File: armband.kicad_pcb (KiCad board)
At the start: 6 copper layers, 151.9 x 110.6 mm, 86 parts, among them IC1 QSMP-1570, IC10 TLE493DW2B6A0HTSA1, IC2 BMI323, IC3 TPS259571DSGR, IC4 TPD6E001RSERG4, IC5 MP2722GRH-0000-Z, IC6 TPS62291DRVR, IC7 TPS62293DRVR, IC8 BQ27427YZFR, IC9 nRF52832-CIAA-G-R7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

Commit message: progressed layout
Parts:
- moved L4 21.9 mm to (149.3, 81.0), turned to 90 degrees
- moved L5 16.3 mm to (149.3, 82.9), turned to 180 degrees
- moved Y2 15.5 mm to (152.8, 83.4)
- moved L6 14.9 mm to (155.4, 79.7), turned to 180 degrees
- moved C33 14.8 mm to (148.1, 82.3), turned to -90 degrees
- moved C32 14.7 mm to (150.4, 82.1), turned to -90 degrees
- moved IC9 14.6 mm to (151.8, 79.5), turned to 180 degrees
- moved C31 13.9 mm to (148.6, 78.6), turned to 90 degrees
- moved C38 13.9 mm to (151.3, 83.6), turned to 90 degrees
- moved C34 13.0 mm to (149.6, 78.6), turned to 90 degrees
- moved AE1 11.3 mm to (157.3, 81.8), turned to -90 degrees
- moved C39 11.1 mm to (154.0, 79.3), turned to 90 degrees
- moved C37 10.8 mm to (154.3, 83.2), turned to -90 degrees
- moved C35 10.8 mm to (151.7, 81.9), turned to 180 degrees
- moved C36 8.96 mm to (154.1, 81.4), turned to 90 degrees
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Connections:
- IC1 pad 19: MP2722_INT -> LCD_TE
- IC1 pad 20: BMI_INT1 -> LCD_RST
- IC1 pad 21: BMI_INT2 -> TP_INT
- IC1 pad 22: MAX_INT -> TP_RST
- IC1 pad 23: TP_INT -> QSMP_LCD_EN
- IC1 pad 24: TP_RST -> BMI_INT1
- IC1 pad 25: LCD_TE -> BMI_INT2
- IC1 pad 26: LCD_RST -> MAX_INT
- IC1 pad 27: QSMP_LCD_EN -> MP2722_INT
- IC9 pad E7: unconnected-(IC9-P0.05/_AIN3-PadE7) -> QSMP_SDA
- IC9 pad F4: QSMP_TXD_NRF -> unconnected-(IC9-P0.11-PadF4)
- IC9 pad F6: QSMP_SDA -> unconnected-(IC9-P0.07-PadF6)
- IC9 pad H3: unconnected-(IC9-P0.16_/TRACEDATA[1]-PadH3) -> QSMP_TXD_NRF
- IC9 pad H4: unconnected-(IC9-P0.15/TRACEDATA[2]-PadH4) -> QSMP_RXD_NRF
- IC9 pad H6: QSMP_RXD_NRF -> unconnected-(IC9-P0.12-PadH6)
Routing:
- net NFC_ANT1: track 0.00 -> 35.1 mm, vias 0 -> 2
- net NFC_ANT2: track 0.00 -> 34.7 mm, vias 0 -> 2
- net TP_INT: track 0.00 -> 33.4 mm, vias 0 -> 2
- net TP_RST: track 0.00 -> 33.4 mm, vias 0 -> 2
- net LCD_RST: track 0.00 -> 33.3 mm, vias 0 -> 2
- net LCD_TE: track 0.00 -> 33.3 mm, vias 0 -> 2
- net QSMP_LCD_EN: track 0.82 -> 32.2 mm, vias 1 -> 2
- net QSMP_RXD_NRF: track 0.00 -> 20.7 mm, vias 0 -> 1
- net QSMP_DCX: track 0.00 -> 19.9 mm, vias 0 -> 1
- net QSMP_TXD_NRF: track 0.00 -> 18.4 mm, vias 0 -> 1
- net QSMP_MISO: track 0.00 -> 14.8 mm, vias 0 -> 1
- net GND: track 4.24 -> 18.7 mm, vias 10 -> 26
- net QSMP_SCK: track 0.00 -> 13.2 mm, vias 0 -> 1
- net QSMP_MOSI: track 0.00 -> 11.9 mm, vias 0 -> 1
- net QSMP_SDA: track 42.3 -> 53.5 mm, vias 3 -> 5
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
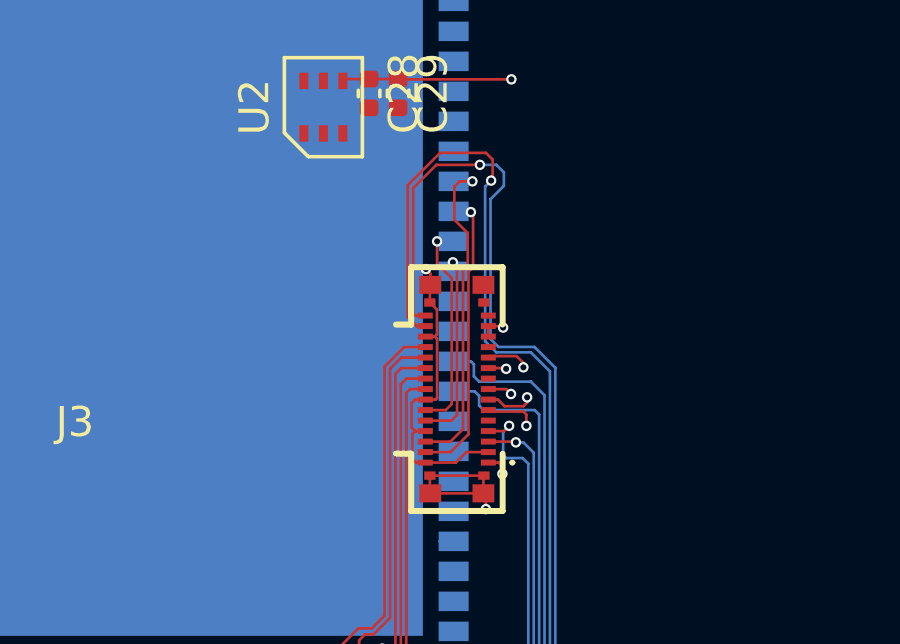
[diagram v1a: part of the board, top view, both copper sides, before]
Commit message: there was an attempt to length match DSI
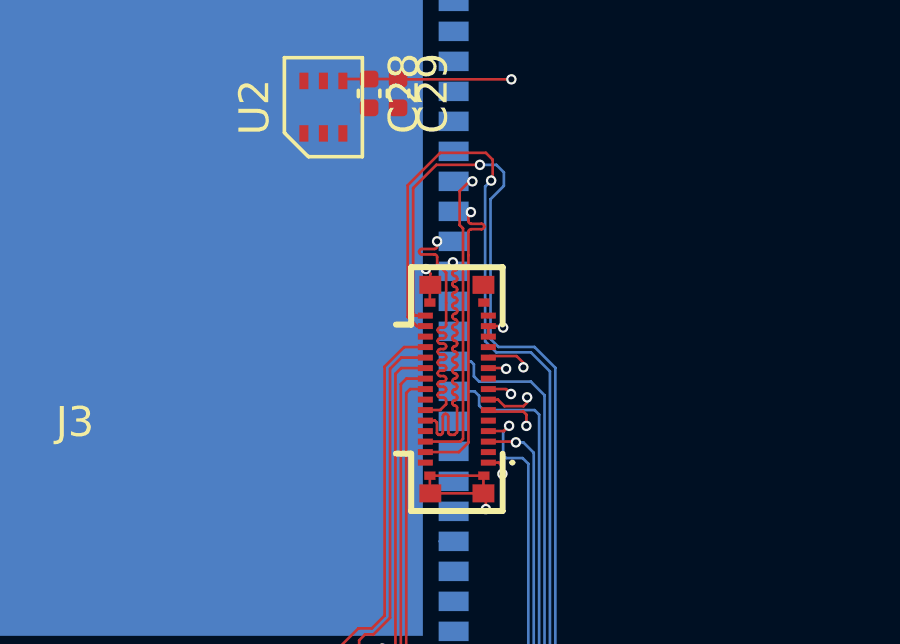
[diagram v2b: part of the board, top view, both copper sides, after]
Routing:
- net GND: track 18.7 -> 9.07 mm
- net QSMP_DSI_CLKN: track 6.59 -> 10.8 mm
- net QSMP_DSI_CLKP: track 7.14 -> 10.6 mm
- net QSMP_DSI_D0N: track 9.77 -> 10.8 mm

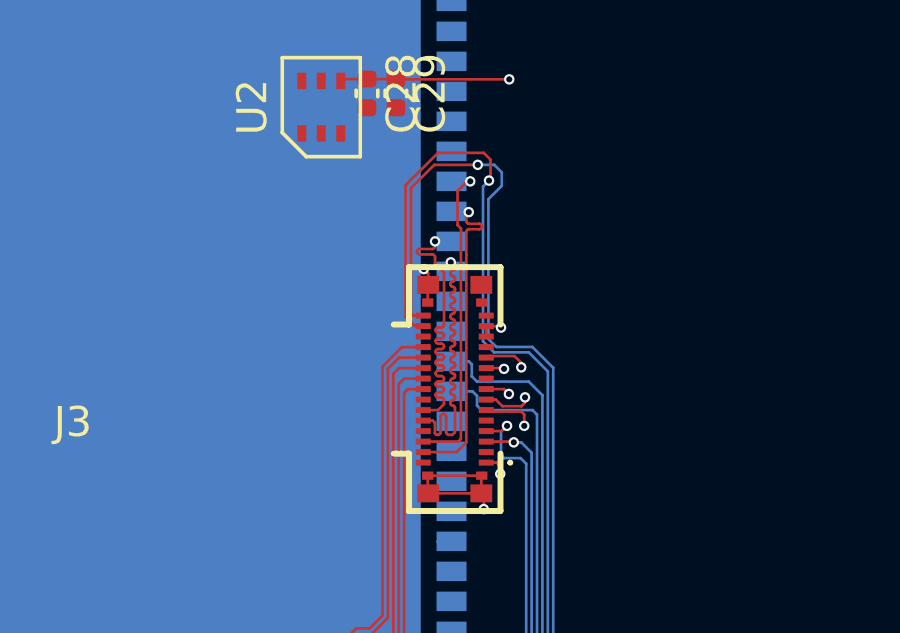
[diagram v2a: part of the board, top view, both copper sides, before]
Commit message: Update length matching
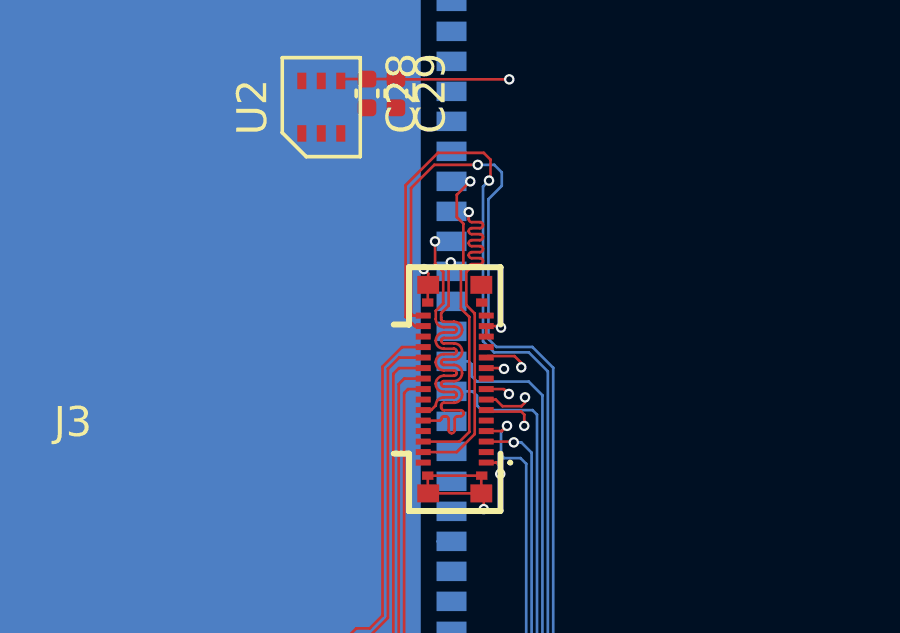
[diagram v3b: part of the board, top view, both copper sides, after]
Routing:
- net QSMP_DSI_D0N: track 10.8 -> 13.1 mm
- net QSMP_DSI_CLKN: track 10.8 -> 12.7 mm

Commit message: progressed layout
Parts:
- moved C10 0.90 mm to (138.8, 84.5)
- moved C11 0.90 mm to (131.8, 85.2)
- moved C12 0.90 mm to (131.8, 81.7)
- moved C13 0.90 mm to (133.5, 85.0)
- moved C14 0.90 mm to (133.5, 86.0)
- moved C15 0.90 mm to (142.8, 86.1)
- moved C16 0.90 mm to (144.7, 81.0)
- moved C17 0.90 mm to (131.8, 79.9)
- moved C21 0.90 mm to (131.8, 83.6)
- moved C22 0.90 mm to (127.6, 79.8)
- moved C23 0.90 mm to (129.0, 79.8)
- moved IC3 0.90 mm to (138.1, 82.7)
- moved IC4 0.90 mm to (141.8, 82.8)
- moved IC5 0.90 mm to (129.4, 82.7)
- moved IC6 0.90 mm to (144.7, 85.4)
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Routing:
- net VSYS: track 36.8 -> 37.7 mm
- net QSMP_SCL: track 52.6 -> 53.5 mm
- net NRF_NRST: track 0.33 -> 0.65 mm, vias 0 -> 1

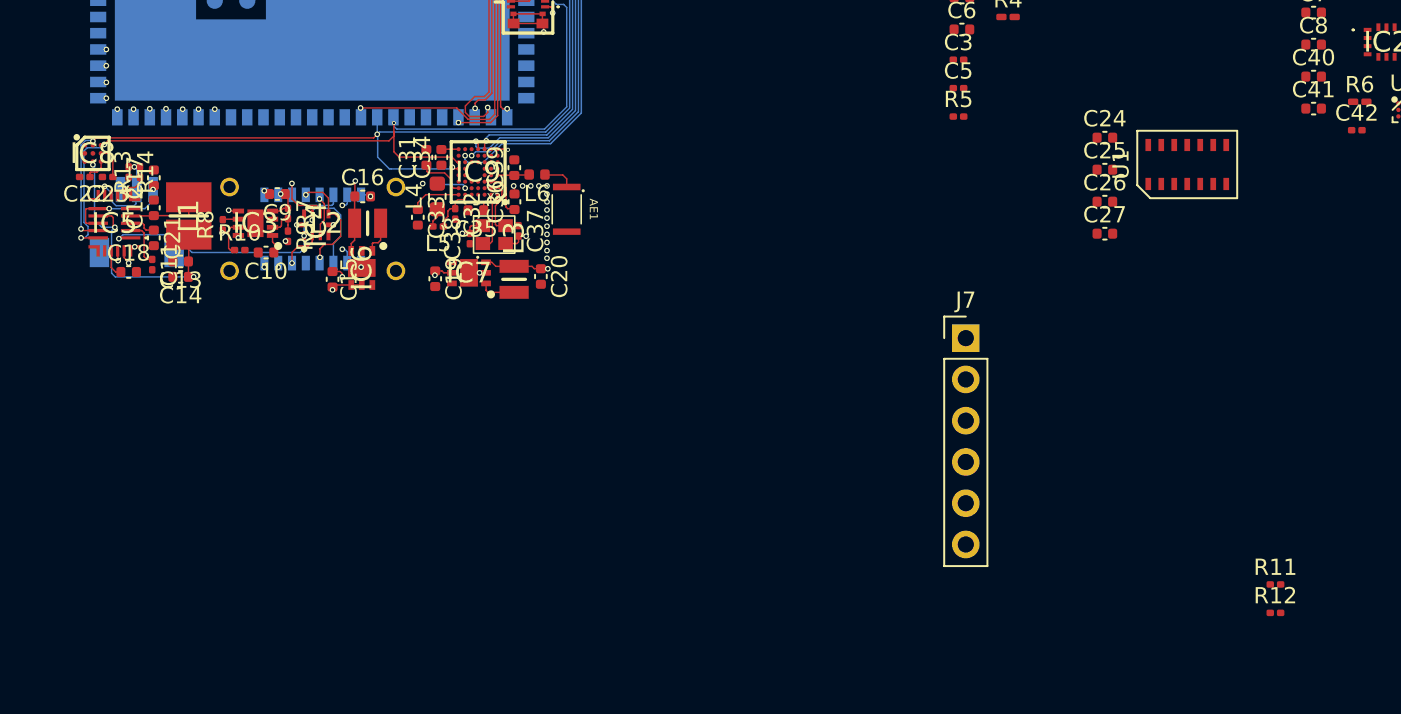
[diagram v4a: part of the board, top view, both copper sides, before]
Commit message: Add Heartbeat sensor to PCB
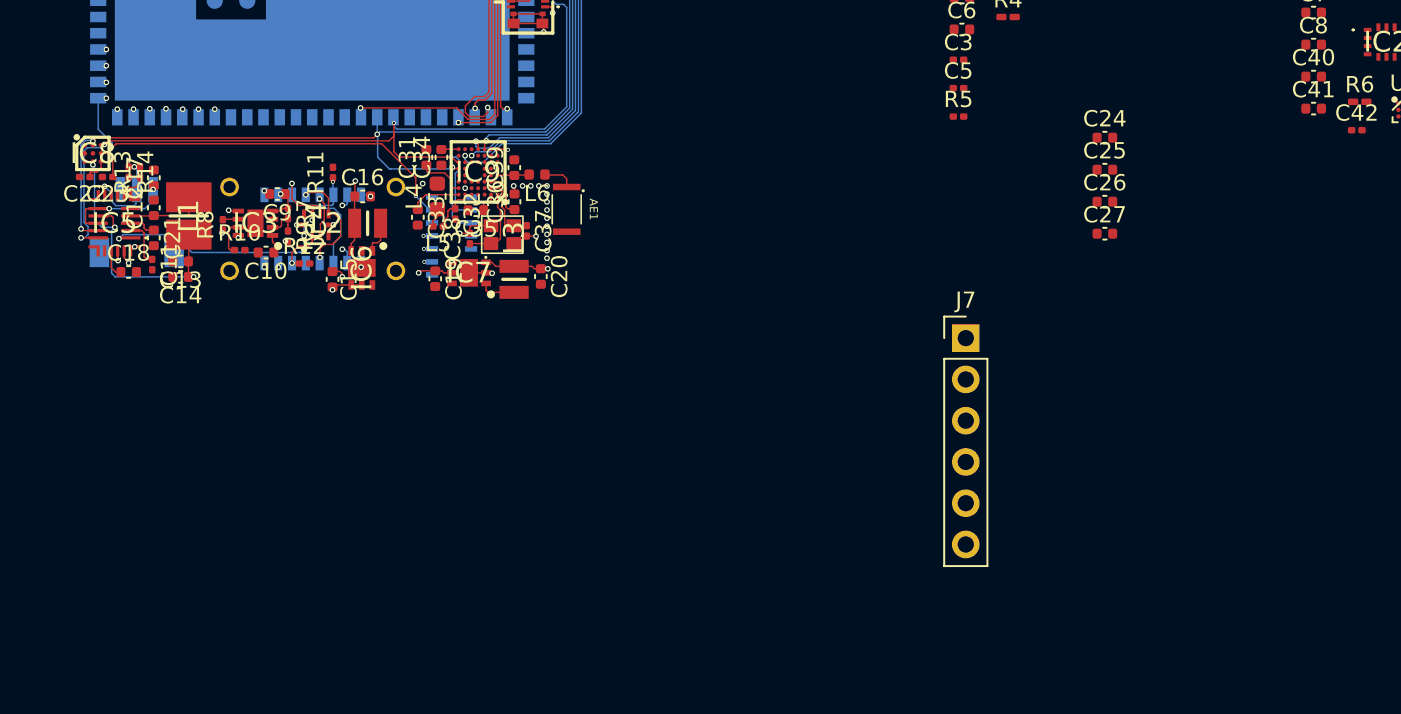
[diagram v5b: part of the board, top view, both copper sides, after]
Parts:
- U1: moved to B.Cu
- moved R12 63.5 mm to (141.1, 85.2)
- moved R11 63.3 mm to (142.9, 79.6), turned to 90 degrees
- moved U1 45.5 mm to (150.2, 83.5), turned to -90 degrees
- moved Y2 0.50 mm to (153.3, 83.4)
- moved C37 0.50 mm to (154.8, 83.2)
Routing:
- net MAX_INT: track 0.50 -> 26.0 mm, vias 1 -> 3
- net QSMP_SCL: track 53.5 -> 58.1 mm, vias 4 -> 5
- net QSMP_SDA: track 53.7 -> 58.1 mm
- net GND: track 9.10 -> 10.4 mm
- net Net-(IC9-XC2): track 3.65 -> 4.84 mm
- net Net-(IC4-IO1): track 18.0 -> 19.1 mm, vias 2 -> 3
- net Net-(IC9-DCC): track 1.89 -> 2.91 mm
- net +3V3: track 16.4 -> 17.4 mm, vias 5 -> 7
- net VSYS: track 37.7 -> 37.0 mm
- net +1V8: track 4.83 -> 5.35 mm, vias 2 -> 3

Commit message: Add debug location
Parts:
- J1: moved to B.Cu
- moved J6 88.3 mm to (117.6, 58.1), turned to 180 degrees
- moved IC2 75.6 mm to (132.1, 72.7), turned to 180 degrees
- moved J1 74.6 mm to (114.8, 62.0), turned to 90 degrees
- moved J2 74.2 mm to (117.6, 68.5), turned to 180 degrees
- moved SW2 70.8 mm to (113.8, 49.3), turned to 90 degrees
- moved SW1 61.8 mm to (122.2, 49.3), turned to 90 degrees
- moved J7 61.4 mm to (122.2, 75.5)
- moved IC10 49.8 mm to (155.6, 56.5), turned to 90 degrees
- moved C30 28.7 mm to (175.7, 58.2)
- moved U3 25.8 mm to (183.2, 74.2)
- moved C40 23.4 mm to (180.6, 67.8)
- moved C7 23.4 mm to (180.6, 63.9)
- moved C8 23.4 mm to (180.6, 65.8)
- moved C41 23.4 mm to (180.6, 69.8)
- moved C42 23.4 mm to (183.3, 71.1)
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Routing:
- net QSMP_SDA: track 58.1 -> 85.6 mm
- net QSMP_SCL: track 58.1 -> 83.9 mm
- net SD_CD: track 0.00 -> 7.48 mm
- net SD_D1: track 0.00 -> 7.44 mm
- net SD_D0: track 0.00 -> 7.40 mm
- net SD_CLK: track 0.00 -> 6.90 mm
- net SD_CMD: track 0.00 -> 6.40 mm
- net SD_D3: track 0.00 -> 6.37 mm
- net SD_D2: track 0.00 -> 6.32 mm

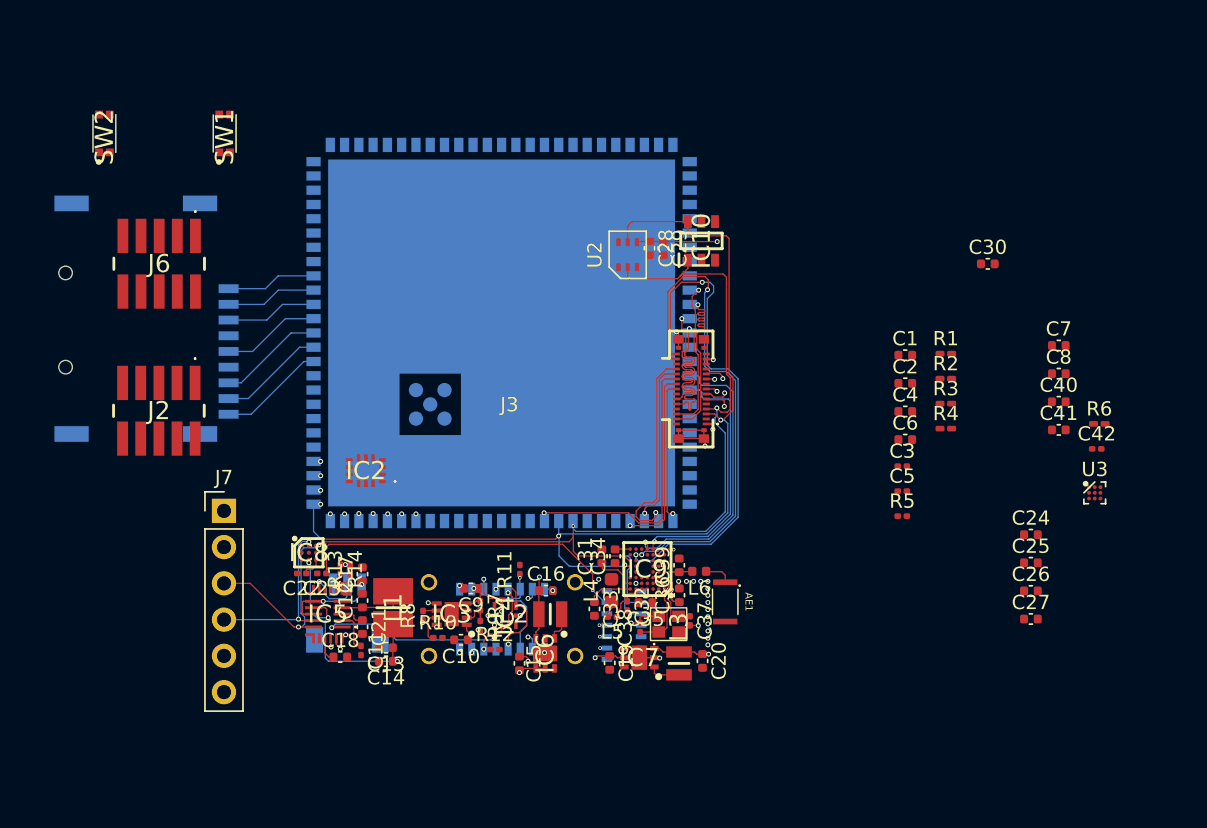
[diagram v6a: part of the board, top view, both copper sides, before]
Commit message: progressed layout and made changes in bmi323 (set unconnected pins to NC) + changed debug connections in preparation to make bridges to debug part + changed VSYS, VUSB, VBAT+ and other connected power traces to 0.2mm trace thickness + added BMI323 layout + moved MAX30102 to make space for caps + added missing caps to MAX30102 + changed gpio order for better layout + added BMM350 layout next to BMI323
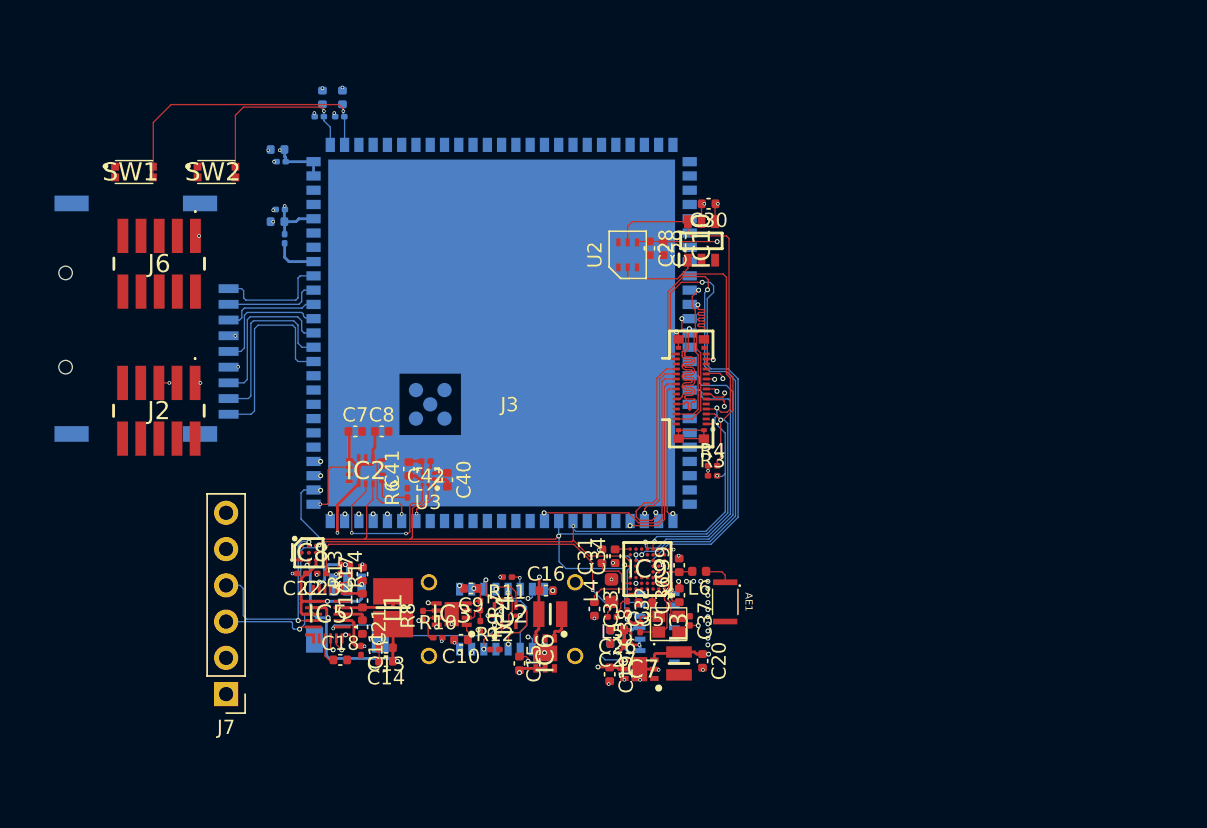
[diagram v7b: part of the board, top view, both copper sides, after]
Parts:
- C1, C2, C24, C25, C3, C4, C5, C6, R5: moved to B.Cu
- R1, R2: footprint Resistor_SMD:R_0201_0603Metric_Pad0.64x0.40mm_HandSolder -> Resistor_SMD:R_0201_0603Metric; moved to B.Cu
- R3, R4, R6: footprint Resistor_SMD:R_0201_0603Metric_Pad0.64x0.40mm_HandSolder -> Resistor_SMD:R_0201_0603Metric
- moved C7 49.6 mm to (131.3, 69.9)
- moved R6 48.7 mm to (135.0, 74.2), turned to 90 degrees
- moved C3 48.5 mm to (126.2, 51.0), turned to 180 degrees
- moved C5 47.8 mm to (126.1, 54.4), turned to 180 degrees
- moved C4 47.6 mm to (125.9, 50.1), turned to 180 degrees
- moved C8 47.6 mm to (133.2, 69.9)
- moved R2 47.6 mm to (128.8, 47.8)
- moved R5 47.4 mm to (126.4, 56.4), turned to -90 degrees
- moved C42 47.0 mm to (136.3, 72.0), turned to 180 degrees
- moved U3 46.7 mm to (136.4, 73.2), turned to 180 degrees
- moved C6 46.6 mm to (125.9, 55.2), turned to 180 degrees
- moved C41 45.6 mm to (135.1, 72.5), turned to 90 degrees
- moved R1 45.6 mm to (130.3, 47.8)
- moved C2 45.5 mm to (129.1, 46.5), turned to 90 degrees
- moved C1 43.4 mm to (130.4, 46.5), turned to 90 degrees
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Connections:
- IC1 pad 19: LCD_TE -> BMM350_INT
- IC1 pad 20: LCD_RST -> BMI_INT1
- IC1 pad 21: TP_INT -> LCD_TE
- IC1 pad 22: TP_RST -> LCD_RST
- IC1 pad 23: QSMP_LCD_EN -> TP_INT
- IC1 pad 24: BMI_INT1 -> TP_RST
- IC1 pad 25: BMI_INT2 -> QSMP_LCD_EN
- IC1 pad 26: MAX_INT -> BMI_INT2
- IC1 pad 27: MP2722_INT -> MAX_INT
- IC1 pad 28: QSMP_BUCK_1V8_EN -> MP2722_INT
- IC1 pad 29: BMM350_INT -> QSMP_BUCK_1V8_EN
- IC2 pad 10: Net-(IC2-NC_1) -> unconnected-(IC2-NC_3-Pad10)
- IC2 pad 11: Net-(IC2-NC_1) -> unconnected-(IC2-NC_4-Pad11)
- IC2 pad 2: Net-(IC2-NC_1) -> unconnected-(IC2-NC_1-Pad2)
- IC2 pad 3: Net-(IC2-NC_1) -> unconnected-(IC2-NC_2-Pad3)
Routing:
- net QSMP_VBUS: track 3.53 -> 53.0 mm, vias 1 -> 3
- net QSMP_BOOT: track 0.00 -> 20.9 mm, vias 0 -> 1
- net GND: track 10.4 -> 26.9 mm, vias 26 -> 53
- net +1V8: track 5.35 -> 21.7 mm, vias 3 -> 4
- net QSMP_SDA: track 85.6 -> 100.3 mm
- net QSMP_NRST: track 0.00 -> 14.1 mm, vias 0 -> 1
- net QSMP_SCL: track 83.9 -> 97.7 mm, vias 5 -> 8
- net +3V3: track 17.4 -> 29.1 mm, vias 7 -> 15
- net SD_CD: track 7.48 -> 14.2 mm
- net BMI_INT1: track 0.50 -> 6.02 mm
- net SD_D1: track 7.44 -> 12.7 mm
- net BMI_INT2: track 0.50 -> 4.95 mm
- net SD_D0: track 7.40 -> 11.2 mm
- net Net-(IC1-USBA_VBUS): track 0.00 -> 3.13 mm
- net Net-(IC2-SDO): track 0.00 -> 2.83 mm
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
